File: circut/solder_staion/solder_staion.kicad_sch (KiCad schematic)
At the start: 0 parts

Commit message: do
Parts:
- added C1: 10nf, symbol Device:C
- added Q1: TSM2302CX, Package_TO_SOT_THT:TO-220-3_Horizontal_TabUp, symbol Transistor_FET:TSM2302CX
- added R1: 10k, symbol Device:R
- added R2: 750k, symbol Device:R
- added R3: 20k, symbol Device:R
- added R4: 30, symbol Device:R
- added R5: Heater, symbol Device:Heater
- added R6, R7: 100, symbol Device:R
- added U1: UC3842_SOIC8, Package_SO:SOIC-8_3.9x4.9mm_P1.27mm, symbol Regulator_Controller:UC3842_SOIC8
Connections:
- new net: R4.1, U1.6 (OUT)
- new net: Q1.1 (G), R4.2
- new net: R1.2, R2.2, U1.2 (FB)
- new net: R2.1, U1.1 (COMP)
- new net: Q1.3 (D), R5.2
- new net: C1.1, R3.2, U1.4 (RC)
- new net +24V: R5.1, U1.7 (VCC)
- new net +5V: R3.1, R6.1, U1.8 (VREF)
- new net GND: C1.2, Q1.2 (S), R7.1, U1.5 (GND)
- new net T+: R1.1
- new net T-: R6.2, R7.2

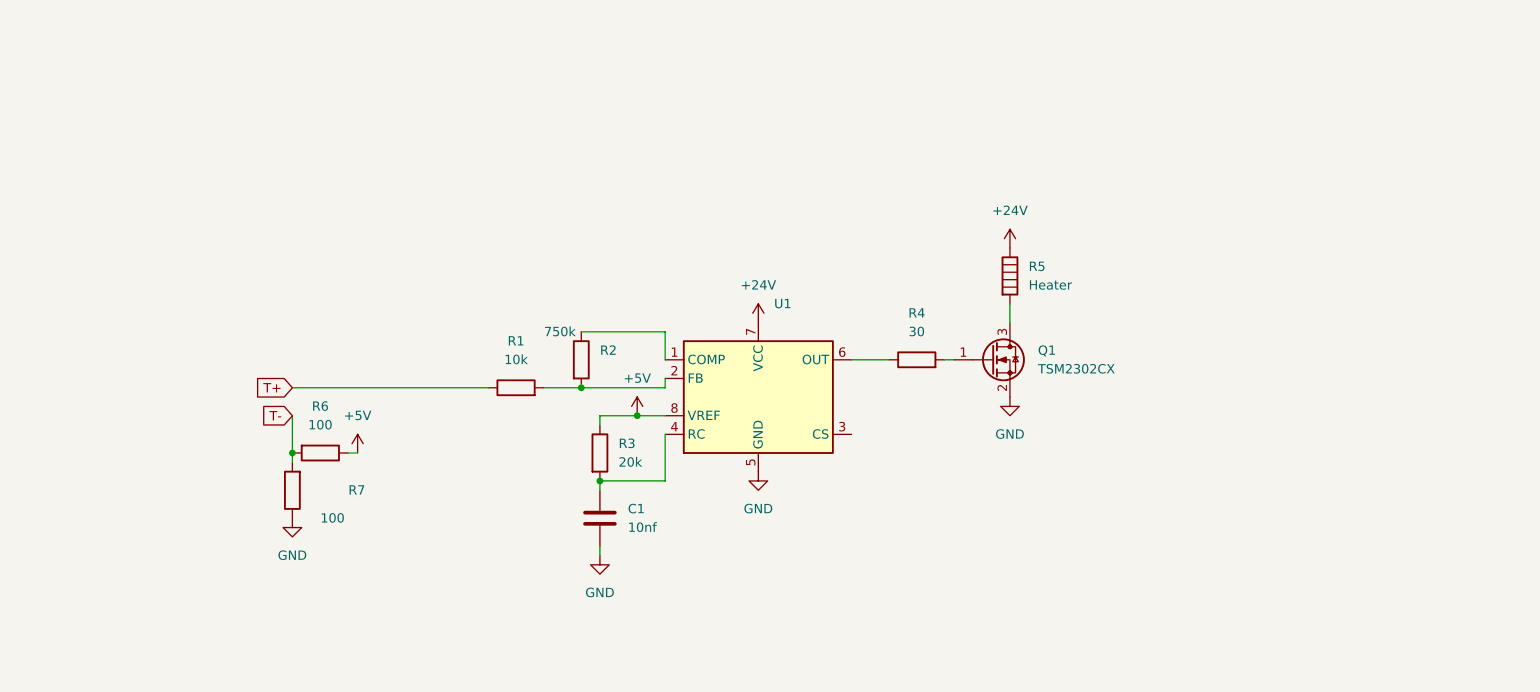
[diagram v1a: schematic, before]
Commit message: Update solder_staion.kicad_sch
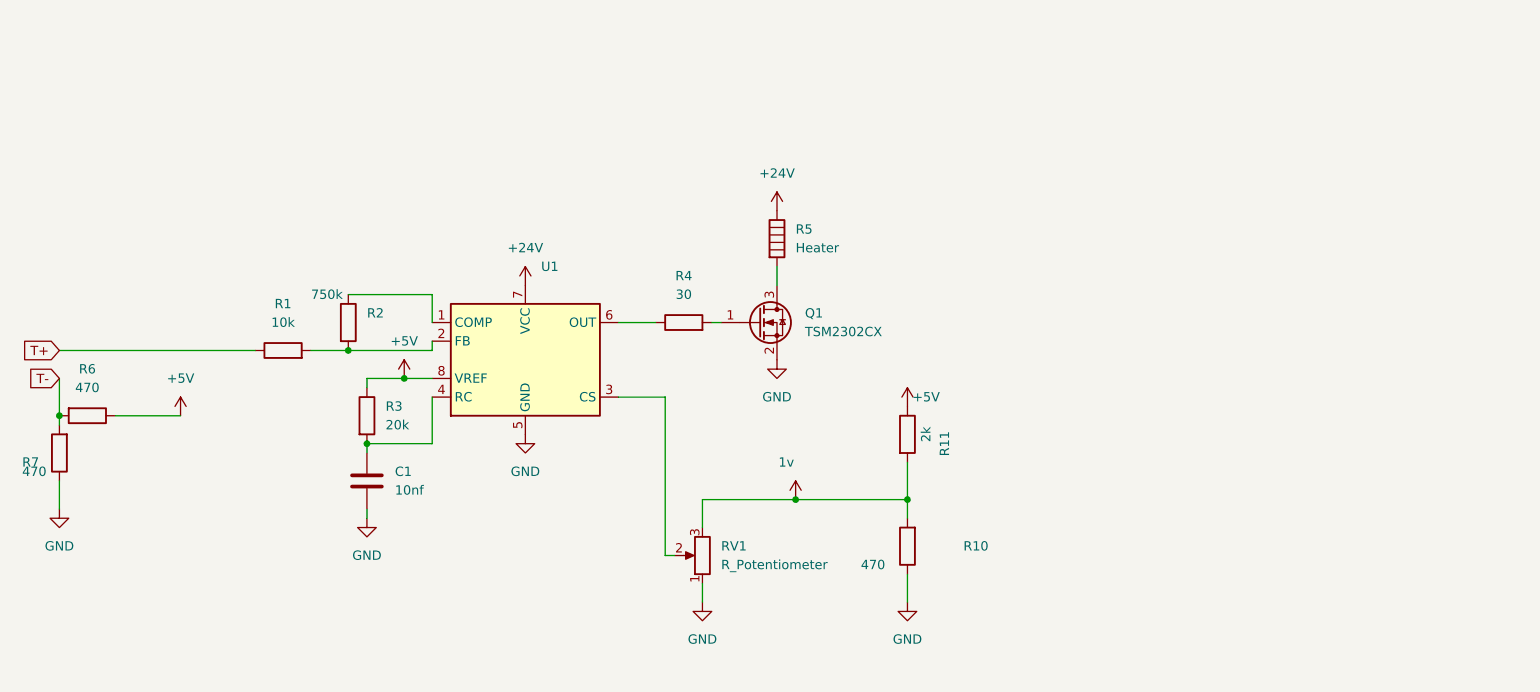
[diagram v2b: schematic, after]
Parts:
- added R10: 470, symbol Device:R
- added R11: 2k, symbol Device:R
- added RV1: R_Potentiometer, symbol Device:R_Potentiometer
- R6, R7: value 100 -> 470
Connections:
- net +5V: now also R11.1
- net GND: now also R10.1, RV1.1
- net at U1.3 (CS): now also RV1.2
- new net 1v: R10.2, R11.2, RV1.3
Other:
- moved on the sheet: C1, Q1, R1, R2, R3, R4, R5, R6, R7, U1

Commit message: Update solder_staion.kicad_sch
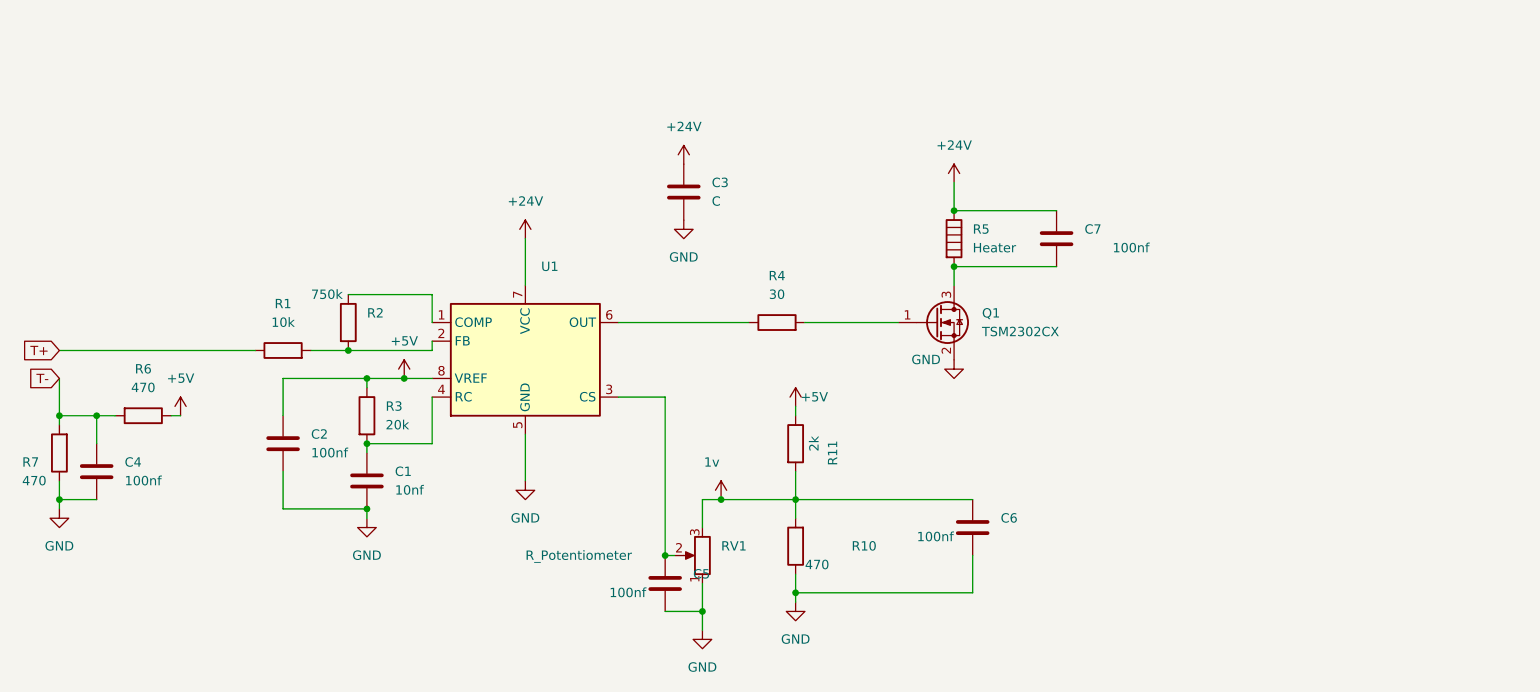
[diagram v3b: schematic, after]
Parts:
- added C2, C4, C5, C6, C7: 100nf, symbol Device:C
- added C3: C, symbol Device:C
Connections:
- net +24V: now also C3.1, C7.1
- net +5V: now also C2.1
- net 1v: now also C6.1
- net GND: now also C2.2, C3.2, C4.2, C5.2, C6.2
- net T-: now also C4.1
- net at RV1.2, U1.3 (CS): now also C5.1
- net at Q1.3 (D), R5.2: now also C7.2
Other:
- moved on the sheet: Q1, R10, R11, R4, R5, R6

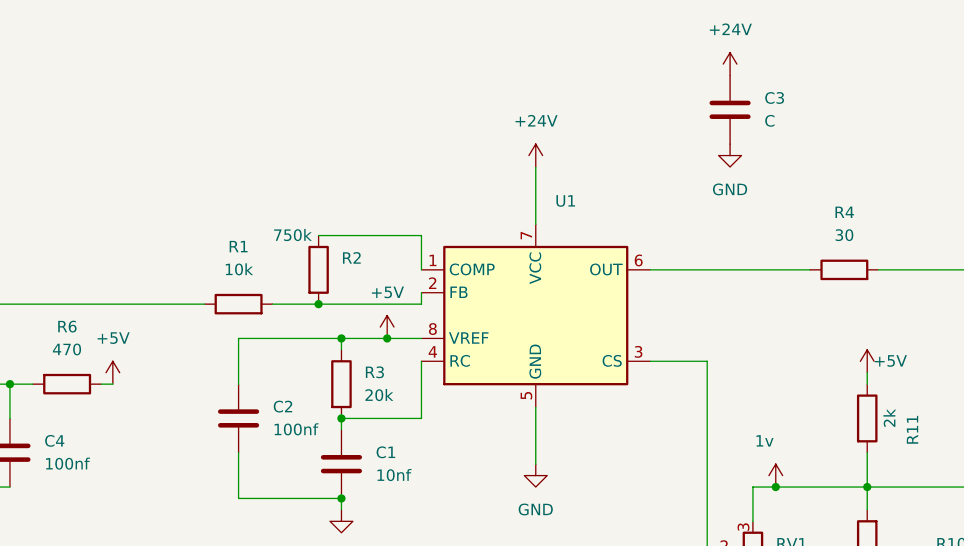
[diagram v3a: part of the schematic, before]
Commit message: Update solder_staion.kicad_sch
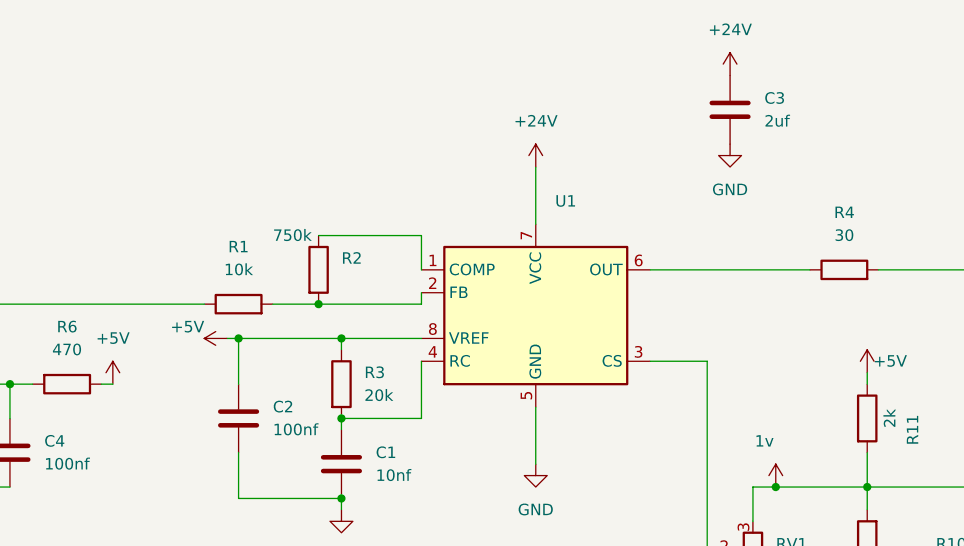
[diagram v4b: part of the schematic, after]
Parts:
- C3: value C -> 2uf
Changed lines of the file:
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@@
+	)
+	(junction
+		(at 95.25 66.04)
+		(diameter 0)
+		(color 0 0 0 0)
 	)
 	(junction
@@
 	)
 	(junction
-		(at 111.76 66.04)
-		(diameter 0)
-		(color 0 0 0 0)
-	)
-	(junction
 		(at 154.94 82.55)
 		(diameter 0)
@@
 	(wire
 		(pts
-			(xy 111.76 66.04) (xy 115.57 66.04)
-		)
-		(stroke
-			(width 0)
-			(type default)
-		)
-	)
-	(wire
-		(pts
 			(xy 104.14 54.61) (xy 115.57 54.61)
 		)
@@
 	(wire
 		(pts
-			(xy 106.68 66.04) (xy 111.76 66.04)
-		)
-		(stroke
-			(width 0)
-			(type default)
-		)
-	)
-	(wire
-		(pts
 			(xy 140.97 58.42) (xy 158.75 58.42)
 		)
@@
 	(wire
 		(pts
-			(xy 95.25 71.12) (xy 95.25 66.04)
-		)
-		(stroke
-			(width 0)
-			(type default)
-		)
-	)
-	(wire
-		(pts
 			(xy 64.77 66.04) (xy 64.77 71.12)
 		)
@@
 	(wire
 		(pts
+			(xy 93.98 66.04) (xy 95.25 66.04)
+		)
+		(stroke
+			(width 0)
+			(type default)
+		)
+	)
+	(wire
+		(pts
 			(xy 115.57 54.61) (xy 115.57 58.42)
 		)
@@
 	(wire
 		(pts
+			(xy 95.25 66.04) (xy 95.25 71.12)
+		)
+		(stroke
+			(width 0)
+			(type default)
+		)
+	)
+	(wire
+		(pts
 			(xy 64.77 82.55) (xy 64.77 83.82)
+		)
+		(stroke
+			(width 0)
+			(type default)
+		)
+	)
+	(wire
+		(pts
+			(xy 106.68 66.04) (xy 115.57 66.04)
 		)
 		(stroke
@@
 	(symbol
 		(lib_id "power:+5V")
-		(at 111.76 66.04 0)
-		(unit 1)
-		(exclude_from_sim no)
-		(in_bom yes)
-		(on_board yes)
-		(dnp no)
-		(fields_autoplaced yes)
+		(at 93.98 66.04 90)
+		(unit 1)
+		(exclude_from_sim no)
+		(in_bom yes)
+		(on_board yes)
+		(dnp no)
 		(property "Reference" "#PWR07"
-			(at 111.76 69.85 0)
+			(at 97.79 66.04 0)
 			(effects
 				(font
@@
 		)
 		(property "Value" "+5V"
-			(at 111.76 60.96 0)
-			(effects
-				(font
-					(size 1.27 1.27)
-				)
-			)
-		)
-		(property "Footprint" ""
-			(at 111.76 66.04 0)
+			(at 91.44 64.77 90)
+			(effects
+				(font
+					(size 1.27 1.27)
+				)
+				(justify left)
+			)
+		)
+		(property "Footprint" ""
+			(at 93.98 66.04 0)
 			(effects
 				(font
@@
 		)
 		(property "Datasheet" ""
-			(at 111.76 66.04 0)
+			(at 93.98 66.04 0)
 			(effects
 				(font
@@
 		)
 		(property "Description" "Power symbol creates a global label with name \"+5V\""
-			(at 111.76 66.04 0)
+			(at 93.98 66.04 0)
 			(effects
 				(font
@@
 			)
 		)
-		(property "Value" "C"
+		(property "Value" "2uf"
 			(at 153.67 41.9099 0)
 			(effects

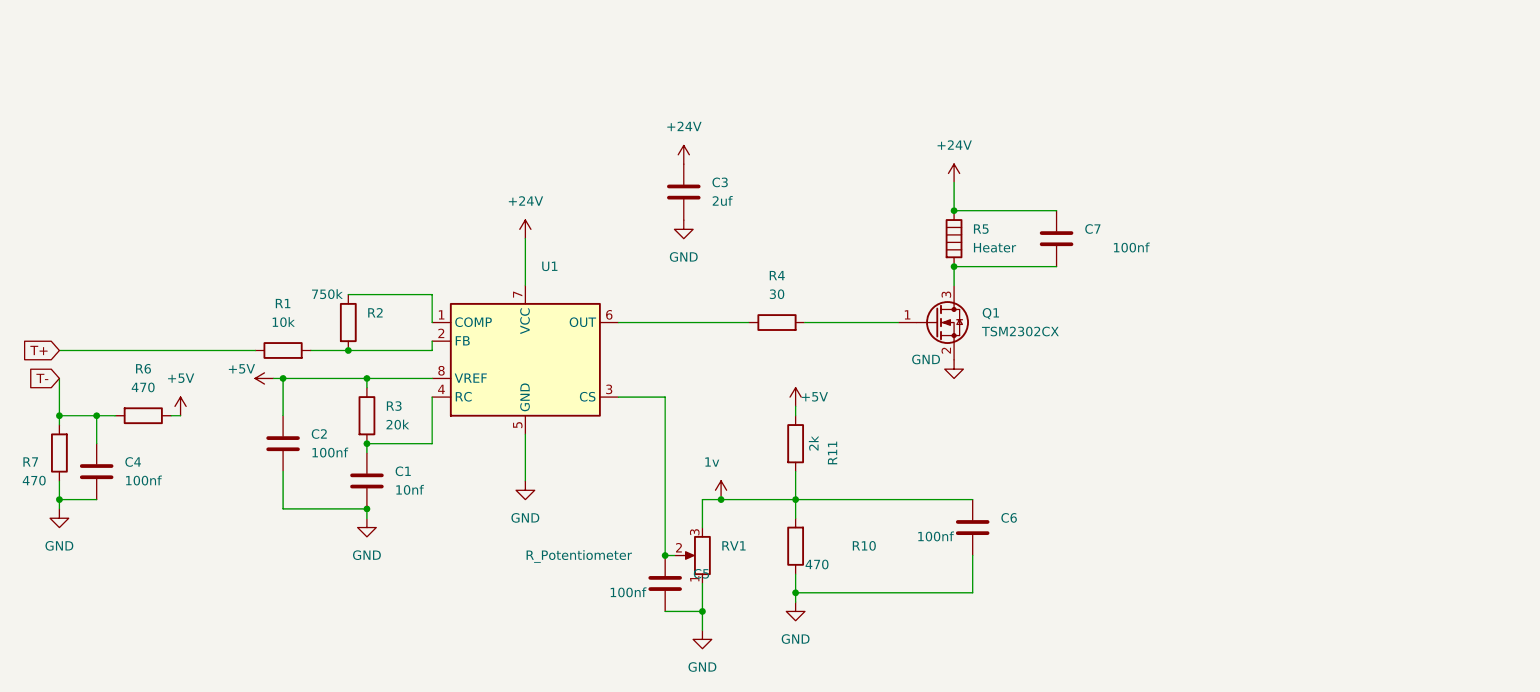
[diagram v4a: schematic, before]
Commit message: Update solder_staion.kicad_sch
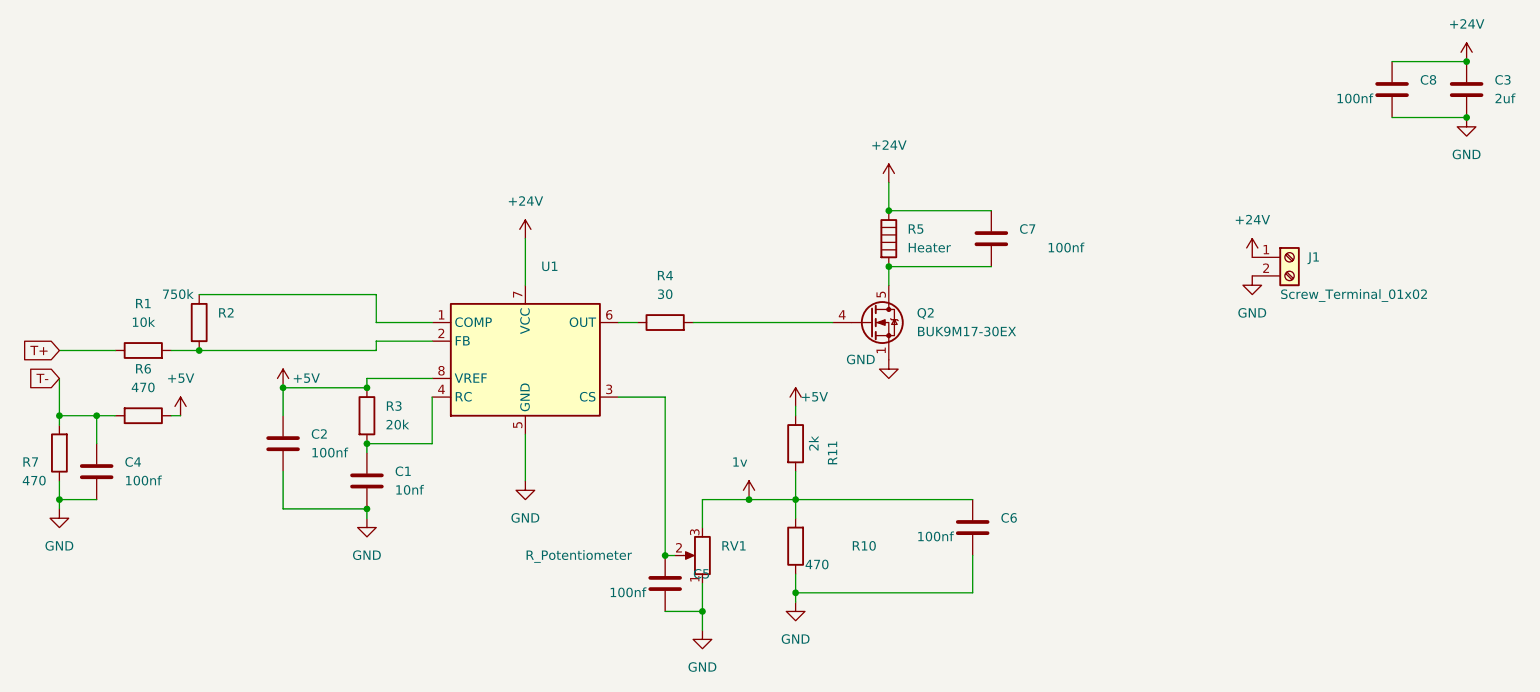
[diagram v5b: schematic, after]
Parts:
- removed Q1: TSM2302CX, Package_TO_SOT_THT:TO-220-3_Horizontal_TabUp, symbol Transistor_FET:TSM2302CX
- added C8: 100nf, symbol Device:C
- added J1: Screw_Terminal_01x02, symbol Connector:Screw_Terminal_01x02
- added Q2: BUK9M17-30EX, Package_TO_SOT_SMD:TDSON-8-1, symbol Transistor_FET:BUK9M17-30EX
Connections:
- net +24V: now also C8.1, J1.1 (Pin_1)
- net GND: now also C8.2, J1.2 (Pin_2), Q2.1 (S), Q2.2 (S), Q2.3 (S)
- net at R4.2: now also Q2.4 (G)
- net at C7.2, R5.2: now also Q2.5 (D)
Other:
- moved on the sheet: C3, C7, R1, R2, R4, R5
